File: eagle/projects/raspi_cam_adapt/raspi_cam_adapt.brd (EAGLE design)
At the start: 21 x 21.2 mm, 4 parts, among them J201 FFC-FPC-15POS, J202 FFC-FPC-15POS, J203 FFC-FPC-15POS

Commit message: finalized panels
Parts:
- removed LOGO1: (no value), daqcs:CMS_LOGO
- added H201, H202: 2.75mm_drill_3.00mm_radius, daqcs:2,75_3,0_HOLE_RASPI
- added LOGO201: (no value), daqcs:CMS_LOGO
- J201: value FFC-FPC-15POS -> FFC-FPC-15POS-BOT
- J202, J203: value FFC-FPC-15POS -> FFC-FPC-15POS-TOP
- moved J201 3.90 mm to (0.00, 14.5)
- moved J202 3.90 mm to (21.0, 14.5)
- moved J203 3.90 mm to (21.0, 14.5)
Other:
- board size 21 x 21.2 mm -> 21 x 29 mm
- board text added: "FROM RASPI"
- board text added: "TO CAM"
- board text removed: "FROM RASPI ZERO"
- board text removed: "TO RASPI CAMERA"

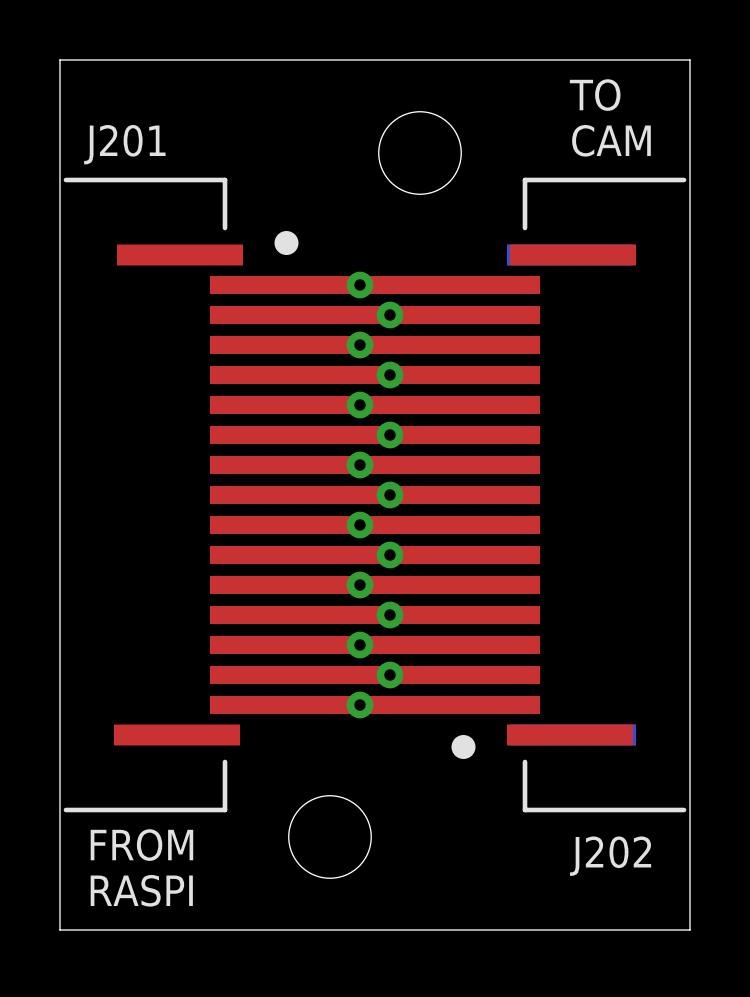
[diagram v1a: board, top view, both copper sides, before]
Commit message: removed inner pours on camera adapte board, re-panneled
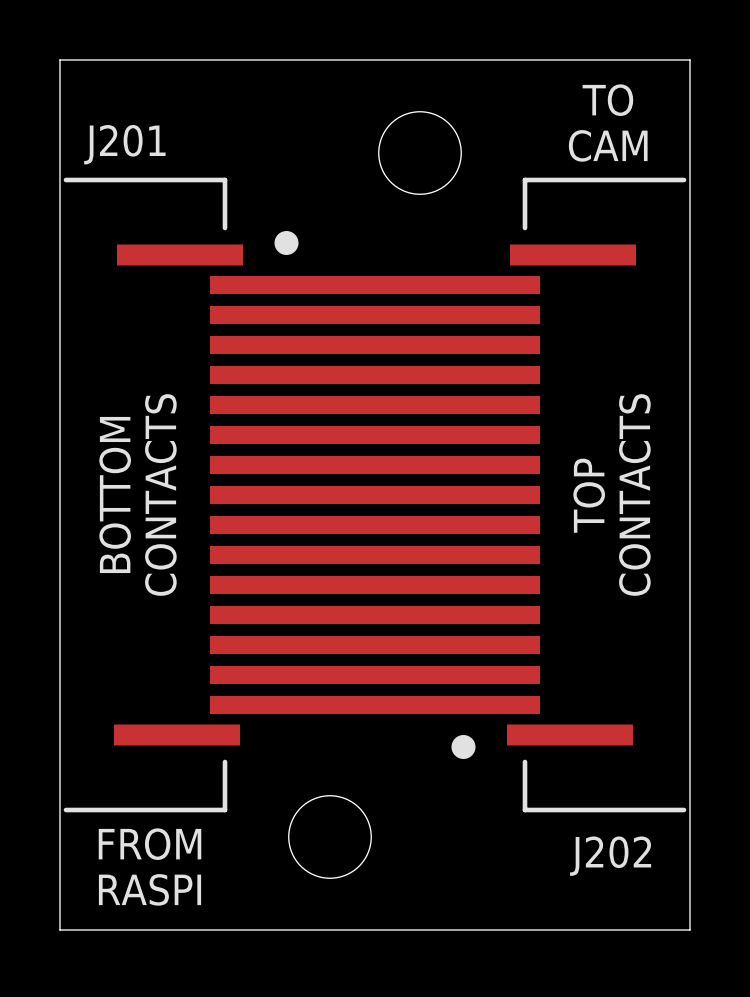
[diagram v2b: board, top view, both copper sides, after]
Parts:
- removed J203: FFC-FPC-15POS-TOP, daqcs:FFC-FPC-100P060X200-15N
- moved LOGO201 16.4 mm to (18.4, 8.44)
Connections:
- removed net GND: J201.1, J201.10, J201.4, J201.7, J202.12, J202.15, J202.6, J202.9, J203.1, J203.10, J203.4, J203.7
- new net GND_1: J201.1, J202.15
- new net GND_2: J201.4, J202.12
- new net GND_3: J201.7, J202.9
- new net GND_4: J201.10, J202.6
- net 3V3: no longer J203.15
- net CAM1_CN: no longer J203.8
- net CAM1_CP: no longer J203.9
- net CAM1_DN0: no longer J203.2
- net CAM1_DN1: no longer J203.5
- net CAM1_DP0: no longer J203.3
- net CAM1_DP1: no longer J203.6
- net CAM_GPIO0: no longer J203.11
- net CAM_GPIO1: no longer J203.12
- net SCL0: no longer J203.13
- net SDA0: no longer J203.14
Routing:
- net GND: track 54.0 -> 0.00 mm, vias 4 -> 0
- net GND_4: track 0.00 -> 9.00 mm
- net GND_3: track 0.00 -> 9.00 mm
- net GND_2: track 0.00 -> 9.00 mm
- net GND_1: track 0.00 -> 9.00 mm
- net SCL0: track 14.0 -> 9.00 mm, vias 1 -> 0
- net CAM_GPIO0: track 14.0 -> 9.00 mm, vias 1 -> 0
- net CAM1_DP0: track 14.0 -> 9.00 mm, vias 1 -> 0
- net CAM1_DN1: track 14.0 -> 9.00 mm, vias 1 -> 0
- net CAM1_CP: track 14.0 -> 9.00 mm, vias 1 -> 0
- net 3V3: track 14.0 -> 9.00 mm, vias 1 -> 0
- net SDA0: track 13.0 -> 9.00 mm, vias 1 -> 0
- net CAM_GPIO1: track 13.0 -> 9.00 mm, vias 1 -> 0
- net CAM1_DP1: track 13.0 -> 9.00 mm, vias 1 -> 0
- net CAM1_DN0: track 13.0 -> 9.00 mm, vias 1 -> 0
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- removed copper zone on layer 15, net GND
- removed copper zone on layer 2, net GND
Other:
- board text added: "BOTTOM CONTACTS"
- board text added: "TOP CONTACTS"
